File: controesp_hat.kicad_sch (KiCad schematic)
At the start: 6 parts, among them J13 Conn_01x19_Socket, J16 Conn_01x19_Socket, J17 Conn_01x19_Socket, U9 PCF8575DBR

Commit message: added part numbers
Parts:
- C4: LCSC (none) -> C49678
- C5: footprint Capacitor_Tantalum_SMD:CP_EIA-7343-31_Kemet-D -> Capacitor_SMD:C_0805_2012Metric_Pad1.18x1.45mm_HandSolder; LCSC (none) -> C15850
- J13, J16, J17: LCSC (none) -> C319202
- U9: LCSC (none) -> C2863388

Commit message: larger pcb
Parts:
- J13, J16, J17: footprint (none) -> Connector_PinHeader_2.54mm:PinHeader_1x19_P2.54mm_Vertical
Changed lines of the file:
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@@
+			"AAAAAAAAAAAAAAAAAAAAAAAAAAAAAAAAAAAAAAAAAAAAAAAAAAAAAAAAAAAAAAAAAAAAAAAAAAAA"
+			"AAAAAAAAAAAAAAAAAAAAAAAAAAAAAAAAAAAAAAAAAAAAAAAAAAAAAAAAAAAAAAAAAAAAAAAAAAAA"
+			"AAAAAAAAAAAAAAAAAAAAAAAAAAAAAAAAAAAAAAAAAAAAAAAAAAAAAAAAAAAAAAAAAAAAAAAAAAAA"
+			"AAAAAAAAAAAAAAAAAAAAAAAAAAAAAAAAAAAAAAAAAAAAAAAAAAAAAAAAAAAAAAAAAAAAAAAAAAAA"
+			"AAAAAAAAAAAAAAAAAAAAAAAAAAAAAAAAAAAAAAAAAAAAAAAAAAAAAAAAAAAAAAAAAAAAAAAAAAAA"
+			"AAAAAAAAAAAAAAAAAAAAAAAAAAAAAAAAAAAAAAAAAAAAAAAAAAAAAAAAAAAAAAAAAAAAAAAAAAAA"
+			"AAAAAAAAAAAAAAAAAAAAAAAAAAAAAAAAAAAAAAAAAAAAAAAAAAAAAAAAAAAAAAAAAAAAAAAAAAAA"
+			"AAAAAAAAAAAAAAAAAAAAAAAAAAAAAAAAAAAAAAAAAAAAAAAAAAAAAAAAAAAAAAAAAAAAAAAAAAAA"
+			"AAAAAAAAAAAAAAAAAAAAAAAAAAAAAAAAAAAAAAAAAAAAAAAAAAAAAAAAAAAAAAAAAAAAAAAAAAAA"
+			"AAAAAAAAAAAAAAAAAAAAAAAAAAAAAAAAAAAAAAAAAAAAAAAAAAAAAAAAAAAAAAAAAAAAAAAAAAAA"
+			"AAAAAAAAAAAAAAAAAAAAAAAAAAAAAAAAAAAAAAAAAAAAAAAAAAAAAAAAAAAAAAAAAAAAAAAAAAAA"
+			"AAAAAAAAAAAAAAAAAAAAAAAAAAAAAAAAAAAAAAAAAAAAAAAAAAAAAAAAAAAAAAAAAAAAAAAAAAAA"
+			"AAAAAAAAAAAAAAAAAAAAAAAAAAAAAAAAAAAAAAAAAAAAAAAAAAAAAAAAAAAAAAAAAAAAAAAAAAAA"
+			"AAAAAAAAAAAAAAAAAAAAAAAAAAAAAAAAAAAAAAAAAAAAAAAAAAAAAAAAAAAAAAAAAAAAAAAAAAAA"
+			"AAAAAAAAAAAAAAAAAAAAAAAAAAAAAAAAAAAAAAAAAAAAAAAAAAAAAAAAAAAAAAAAAAAAAAAAAAAA"
+			"AAAAAAAAAAAAAAAAAAAAAAAAAAAAAAAAAAAAAAAAAAAAAAAAAAAAAAAAAAAAAAAAAAAAAAAAAAAA"
+			"AAAAAAAAAAAAAAAAAAAAAAAAAAAAAAAAAAAAAAAAAAAAAAAAAAAAAAAAAAAAAAAAAAAAAAAAAAAA"
+			"AAAAAAAAAAAAAAAAAAAAAAAAAAAAAAAAAAAAAAAAAAAAAAAAAAAAAAAAAAAAAAAAAAAAAAAAAAAA"
 			"AAAAAAAAAAAAAAAAAAAAAAAAAAAAAAAAAAAAAAAAAAAAAAAAAAAAAAAAAAAAAAAAAAAAAAAAAAAA"
 			"AAAAAAAAAAAAAAAAAAAAAAAAAAAAAAAAAAAAAAAAAAAAAAAAAAAAAAAAAAAAAAAAAAAAAAAAAAAA"
@@
 			)
 		)
-		(property "Footprint" ""
+		(property "Footprint" "Connector_PinHeader_2.54mm:PinHeader_1x19_P2.54mm_Vertical"
 			(at 83.82 78.74 0)
 			(effects
@@
 			)
 		)
-		(property "Footprint" ""
+		(property "Footprint" "Connector_PinHeader_2.54mm:PinHeader_1x19_P2.54mm_Vertical"
 			(at 20.32 78.74 0)
 			(effects
@@
 			)
 		)
-		(property "Footprint" ""
+		(property "Footprint" "Connector_PinHeader_2.54mm:PinHeader_1x19_P2.54mm_Vertical"
 			(at 58.42 78.74 0)
 			(effects

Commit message: added fuse and c for 7805
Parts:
- added C1, C2: 100nF, Capacitor_SMD:C_0805_2012Metric_Pad1.18x1.45mm_HandSolder, symbol Device:C
- added U3: TCA9517ADGK, Package_SO:VSSOP-8_3x3mm_P0.65mm, symbol Logic_LevelTranslator:TCA9517ADGK
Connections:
- net 3V3: now also C1.1, U3.8 (VCCB)
- net SCL: now also U3.7 (SCLB); no longer U9.22 (SCL)
- net SDA: now also U3.6 (SDAB); no longer U9.23 (SDA)
- net GND_hat renamed GND
- net GND: now also C1.2, C2.2, U3.4 (GND)
- net VCC_hat renamed VCC
- net VCC: now also C2.1, U3.1 (VCCA)
- new net SCL_5V: U3.2 (SCLA), U9.22 (SCL)
- new net SDA_5V: U3.3 (SDAA), U9.23 (SDA)
- no-connect marks 17 -> 18
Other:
- moved on the sheet: C4, C5

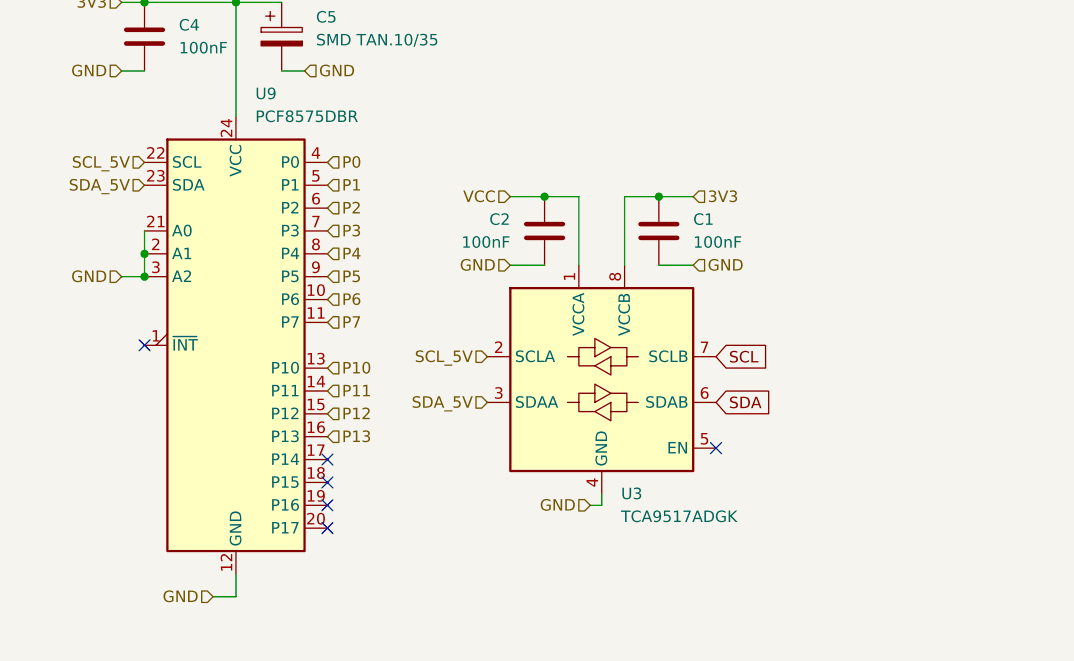
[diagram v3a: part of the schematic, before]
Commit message: hat routing finished
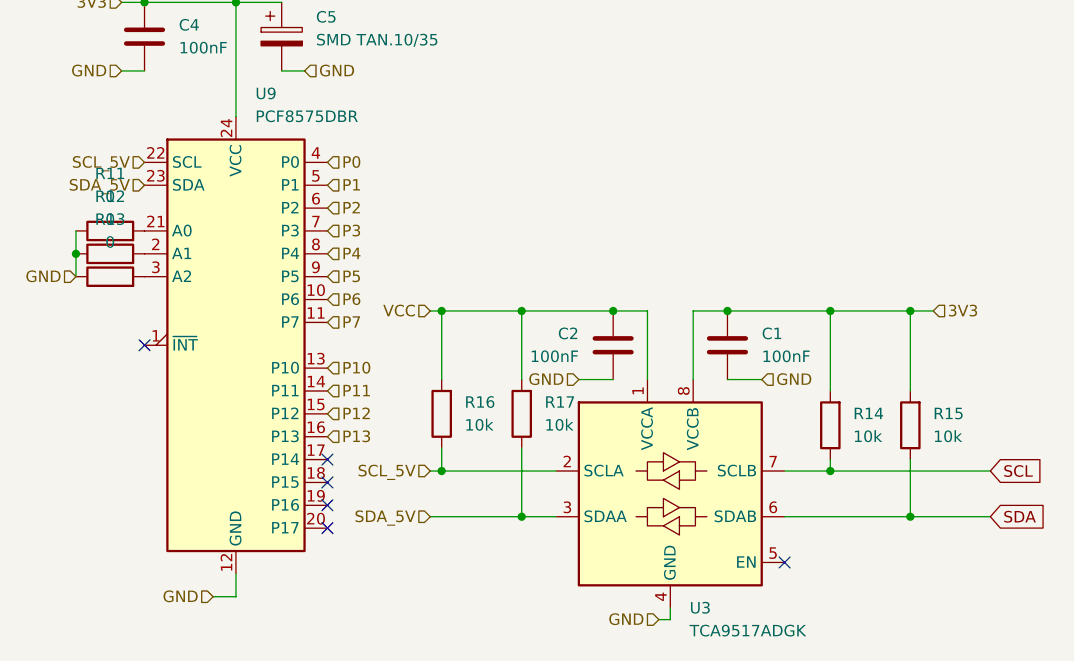
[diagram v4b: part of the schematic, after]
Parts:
- added R11, R12, R13: 0, Resistor_SMD:R_0805_2012Metric_Pad1.20x1.40mm_HandSolder, symbol Device:R
- added R14, R15, R16, R17: 10k, Resistor_SMD:R_0805_2012Metric_Pad1.20x1.40mm_HandSolder, symbol Device:R
- J13, J16, J17: footprint Connector_PinHeader_2.54mm:PinHeader_1x19_P2.54mm_Vertical -> Connector_PinSocket_2.54mm:PinSocket_1x19_P2.54mm_Vertical
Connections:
- net 3V3: now also R14.2, R15.2
- net GND: now also R11.1, R12.1, R13.1; no longer U9.2 (A1), U9.21 (A0), U9.3 (A2)
- net SCL: now also R14.1
- net SCL_5V: now also R16.1
- net SDA: now also R15.1
- net SDA_5V: now also R17.1
- net VCC: now also R16.2, R17.2
- new net: R13.2, U9.3 (A2)
- new net: R12.2, U9.2 (A1)
- new net: R11.2, U9.21 (A0)
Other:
- moved on the sheet: C1, C2, U3

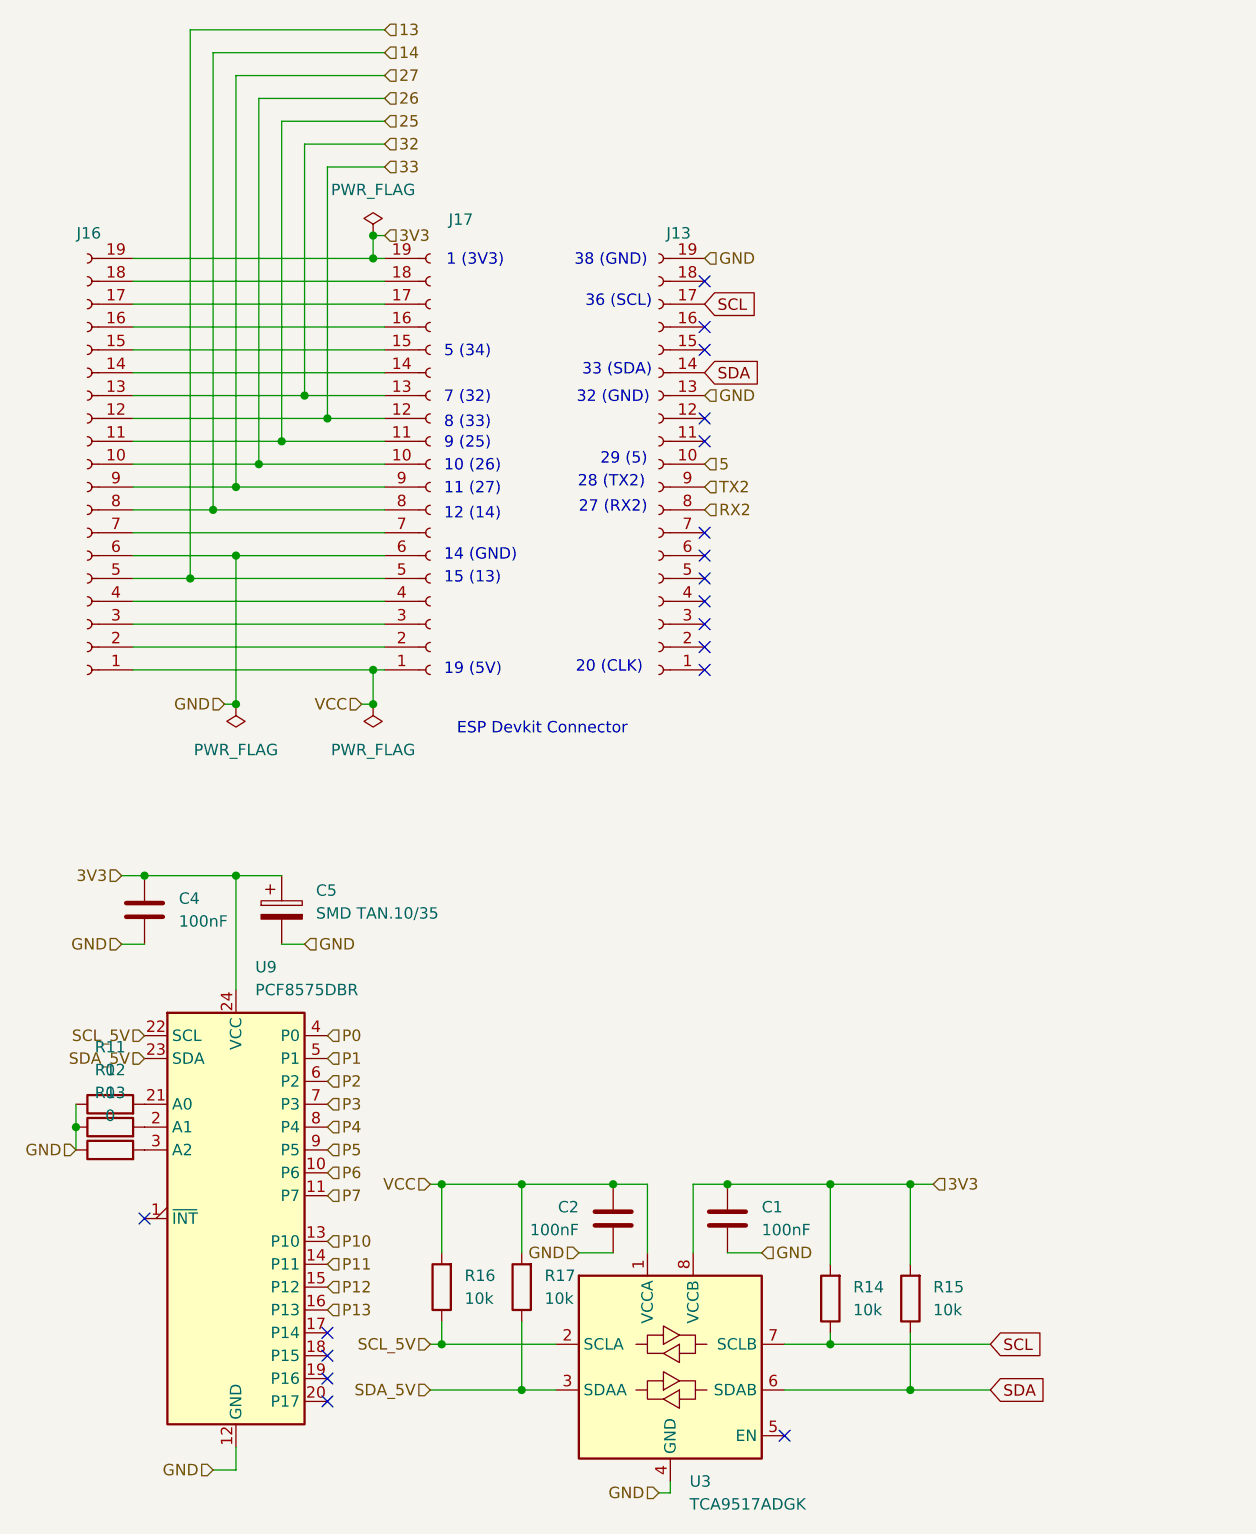
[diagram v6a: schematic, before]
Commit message: pcb layout finished
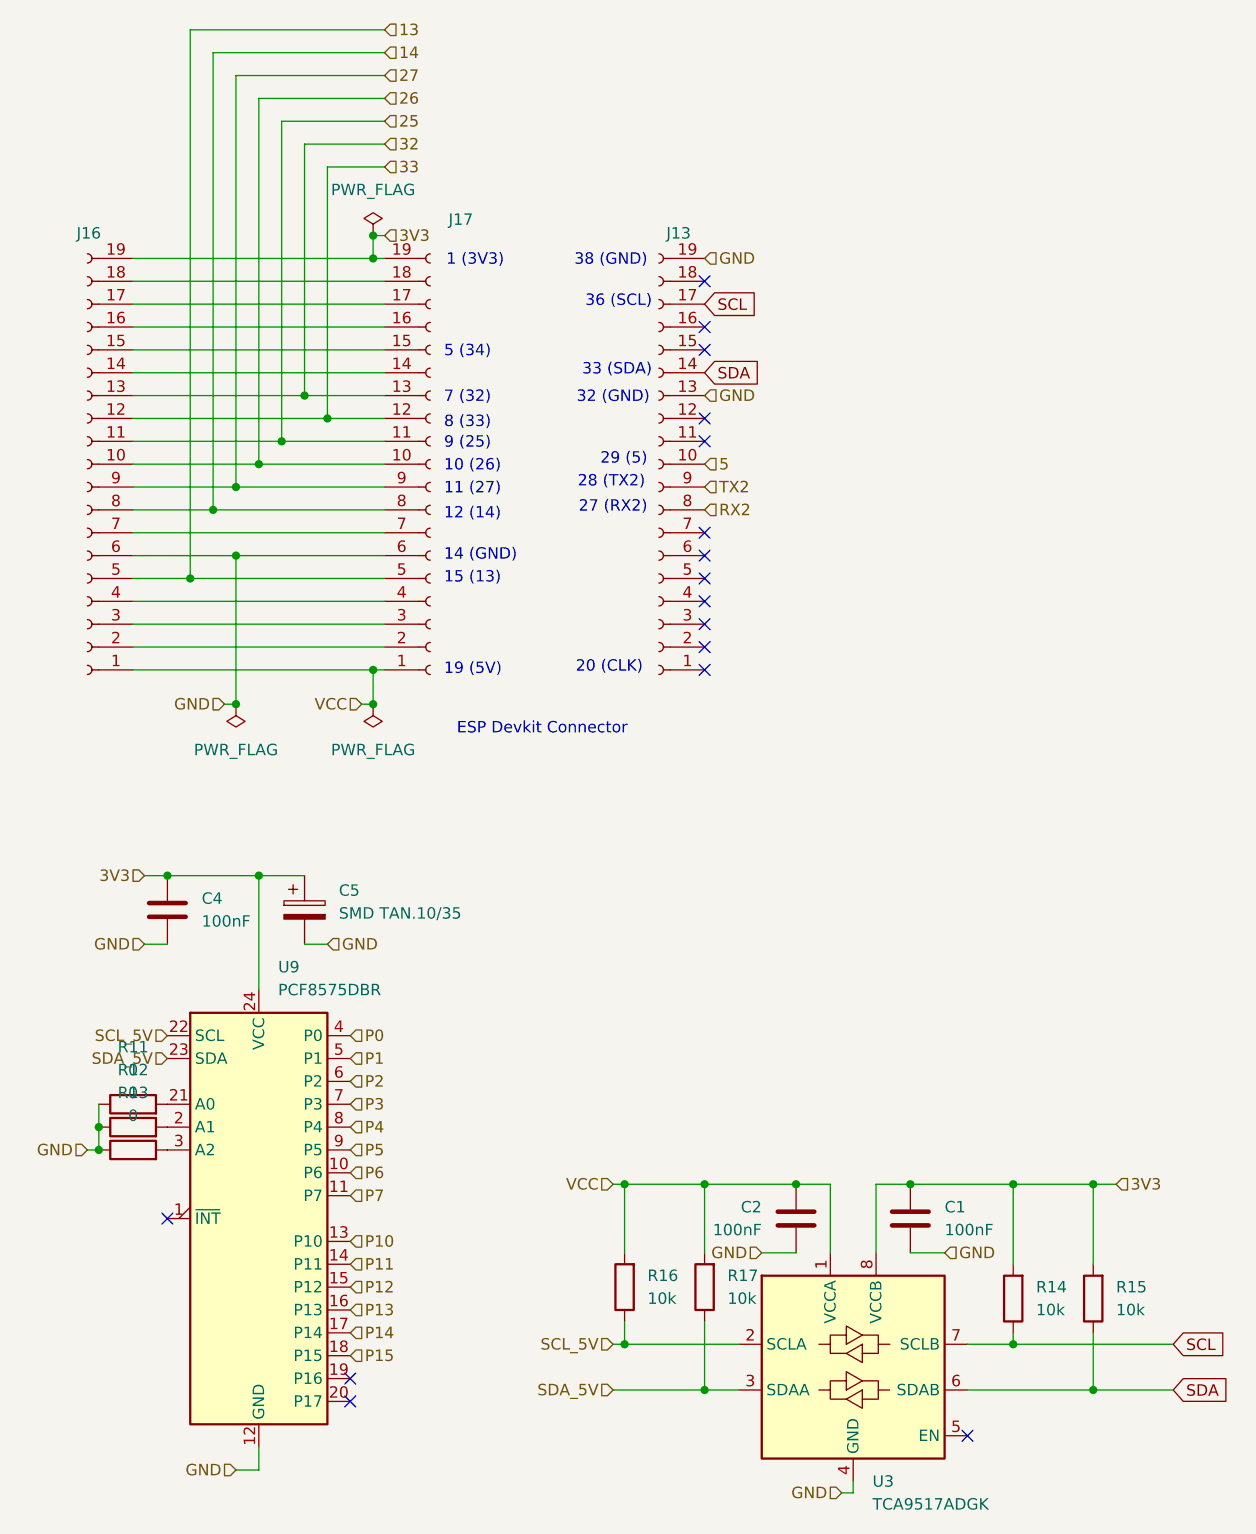
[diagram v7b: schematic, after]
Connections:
- net P14: now reaches U9.17 (P14)
- net P15: now reaches U9.18 (P15)
- no-connect marks 18 -> 16
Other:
- moved on the sheet: C1, C2, C4, C5, R11, R12, R13, R14, R15, R16, R17, U3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
